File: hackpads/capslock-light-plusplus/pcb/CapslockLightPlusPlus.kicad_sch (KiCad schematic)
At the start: 21 parts, among them J0 Conn_01x03_Socket, J1 Conn_01x04, SW0 SW_Push, SW1 SW_Push, SW2 SW_Push, SW3 SW_Push, SW4 SW_Push, SW5 SW_Push, SW6 RotaryEncoder_Switch_MP, SW7 SW_Push, SW8 SW_Push, U0 Seeed Studio XIAO SAMD21

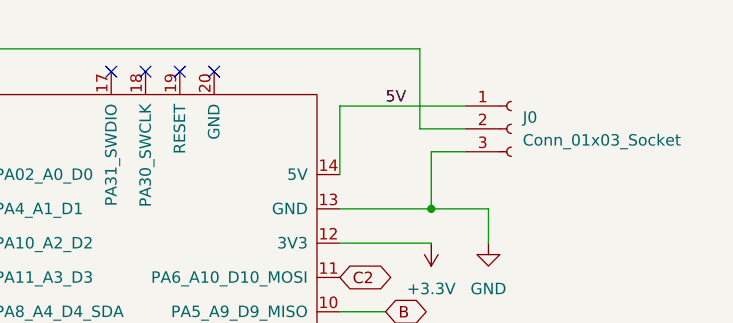
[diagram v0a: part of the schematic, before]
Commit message: Minior changes to the pcb to remove SMD pads, OLED changes
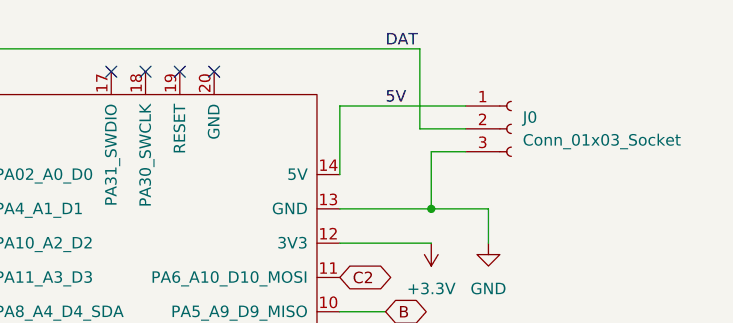
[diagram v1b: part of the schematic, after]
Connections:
- net DAT: now reaches J0.2 (Pin_2), U0.1 (PA02_A0_D0)
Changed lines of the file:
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@@
+		)
+	)
+	(label "DAT"
+		(at 237.49 29.21 0)
+		(fields_autoplaced yes)
+		(effects
+			(font
+				(size 1.27 1.27)
+			)
+			(justify left bottom)
 		)
 	)
